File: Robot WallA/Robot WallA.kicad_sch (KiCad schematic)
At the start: 4 parts

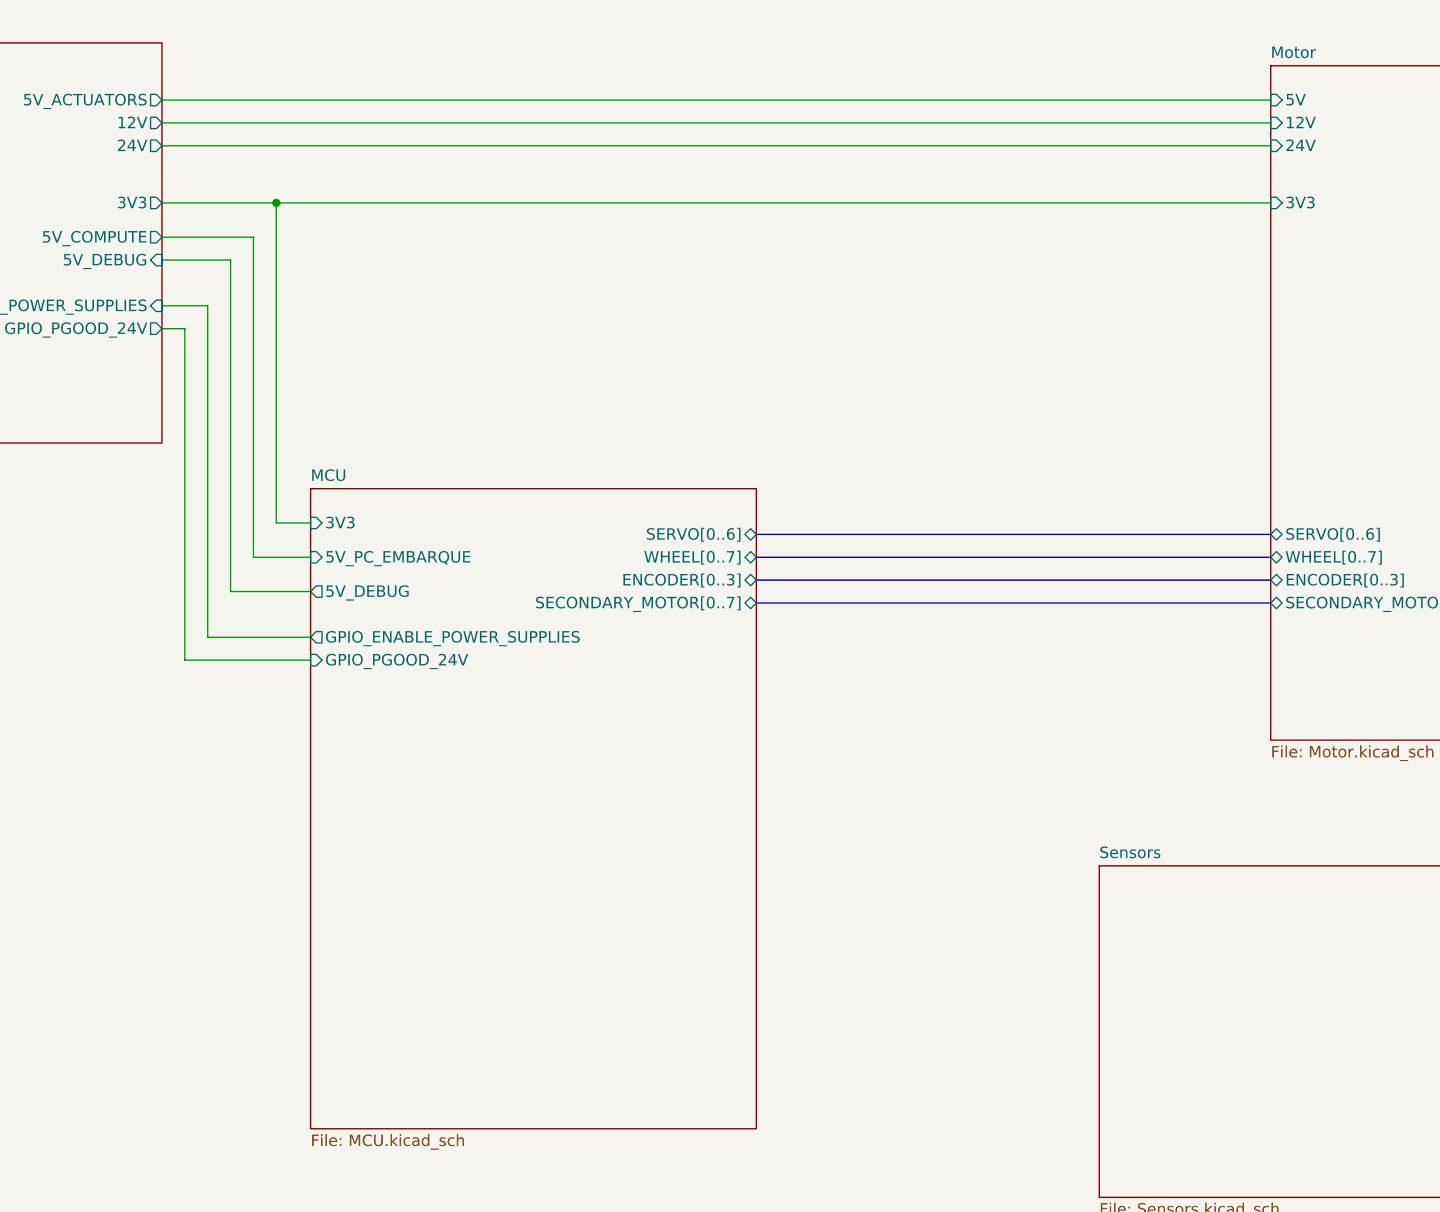
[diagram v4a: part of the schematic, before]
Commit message: Updated USB UART converter, Linked telemeter sensors.
Updated components indicators
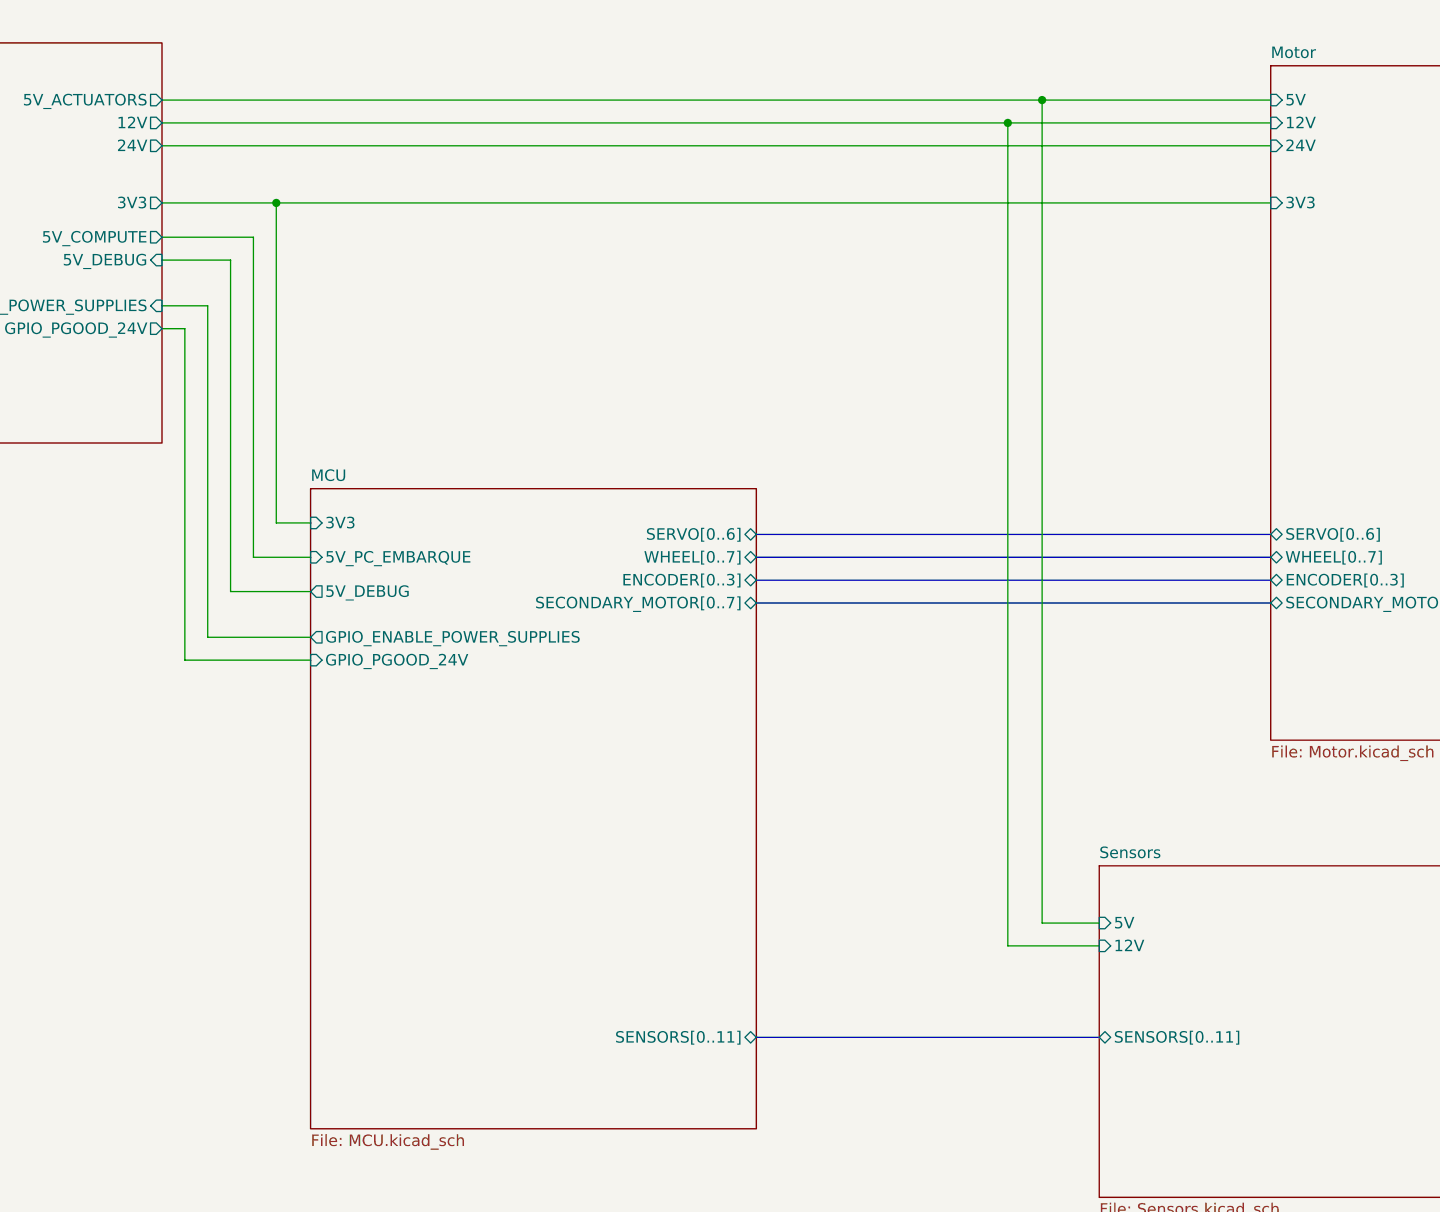
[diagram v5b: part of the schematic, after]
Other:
- sheet MCU ports: added SENSORS[0..11]; removed none
- sheet Sensors ports: added 12V, 5V, SENSORS[0..11]; removed none
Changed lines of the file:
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@@
+	)
+	(junction
+		(at 203.2 25.4)
+		(diameter 0)
+		(color 0 0 0 0)
 	)
 	(junction
@@
 		(color 0 0 0 0)
 	)
-	(wire
-		(pts
-			(xy 109.22 25.4) (xy 232.41 25.4)
+	(junction
+		(at 207.01 22.86)
+		(diameter 0)
+		(color 0 0 0 0)
+	)
+	(wire
+		(pts
+			(xy 109.22 25.4) (xy 203.2 25.4)
 		)
 		(stroke
@@
 	(wire
 		(pts
+			(xy 203.2 25.4) (xy 232.41 25.4)
+		)
+		(stroke
+			(width 0)
+			(type default)
+		)
+	)
+	(wire
+		(pts
 			(xy 109.22 34.29) (xy 121.92 34.29)
 		)
@@
 	(wire
 		(pts
+			(xy 213.36 116.84) (xy 203.2 116.84)
+		)
+		(stroke
+			(width 0)
+			(type default)
+		)
+	)
+	(wire
+		(pts
+			(xy 213.36 114.3) (xy 207.01 114.3)
+		)
+		(stroke
+			(width 0)
+			(type default)
+		)
+	)
+	(wire
+		(pts
 			(xy 125.73 82.55) (xy 114.3 82.55)
 		)
@@
 	(wire
 		(pts
+			(xy 203.2 116.84) (xy 203.2 25.4)
+		)
+		(stroke
+			(width 0)
+			(type default)
+		)
+	)
+	(bus
+		(pts
+			(xy 175.26 127) (xy 213.36 127)
+		)
+		(stroke
+			(width 0)
+			(type default)
+		)
+	)
+	(wire
+		(pts
 			(xy 232.41 34.29) (xy 121.92 34.29)
 		)
@@
 	(wire
 		(pts
+			(xy 207.01 114.3) (xy 207.01 22.86)
+		)
+		(stroke
+			(width 0)
+			(type default)
+		)
+	)
+	(wire
+		(pts
 			(xy 119.38 73.66) (xy 125.73 73.66)
 		)
@@
 	(wire
 		(pts
-			(xy 109.22 22.86) (xy 232.41 22.86)
+			(xy 207.01 22.86) (xy 232.41 22.86)
+		)
+		(stroke
+			(width 0)
+			(type default)
+		)
+	)
+	(wire
+		(pts
+			(xy 109.22 22.86) (xy 207.01 22.86)
 		)
 		(stroke
@@
 			)
 		)
+		(pin "SENSORS[0..11]" bidirectional
+			(at 213.36 127 180)
+			(effects
+				(font
+					(size 1.27 1.27)
+				)
+				(justify left)
+			)
+		)
+		(pin "5V" input
+			(at 213.36 114.3 180)
+			(effects
+				(font
+					(size 1.27 1.27)
+				)
+				(justify left)
+			)
+		)
+		(pin "12V" input
+			(at 213.36 116.84 180)
+			(effects
+				(font
+					(size 1.27 1.27)
+				)
+				(justify left)
+			)
+		)
 		(instances
 			(project "Robot WallA"
@@
 			(effects
 				(font
+					(size 1.27 1.27)
+				)
+				(justify right)
+			)
+		)
+		(pin "SENSORS[0..11]" bidirectional
+			(at 175.26 127 0)
+			(effects
+				(font

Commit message: Added standard switchs, debug leds and 12V and 5V connectors
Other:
- sheet MCU ports: added SENSORS[0..15]; removed SENSORS[0..11]
- sheet Sensors ports: added SENSORS[0..15]; removed SENSORS[0..11]
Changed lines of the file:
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@@
 	(wire
 		(pts
-			(xy 232.41 34.29) (xy 121.92 34.29)
+			(xy 121.92 34.29) (xy 232.41 34.29)
 		)
 		(stroke
@@
 			)
 		)
-		(pin "SENSORS[0..11]" bidirectional
+		(pin "SENSORS[0..15]" bidirectional
 			(at 213.36 127 180)
 			(effects
@@
 			)
 		)
-		(pin "SENSORS[0..11]" bidirectional
+		(pin "SENSORS[0..15]" bidirectional
 			(at 175.26 127 0)
 			(effects

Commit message: Begin to route ethenet, usb, 24V power supply.
Reworked Ethernet sheet because it was too hard to read
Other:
- note added: "Manufacturer: JLCPCB 4 layers 1.6mm 2oz outer layer 0.5oz inner layer https://jlcpcb.com/impedance https://jlcpcb.com/capabilities/pcb-capabilities"
- note added: "PCB Recommendations: FR-4 Glass Epoxy material with 2 oz. (70 μm) copper on both top and bottom layer is recommended for improved thermal performance and better EMI margin (due to lower PCB trace inductance). (From Motor Driver DRV8262 datasheet page 46)"
- note removed: "PCB Recommendations: FR-4 Glass Epoxy material with 2 oz. (70 μm) copper on both top and bottom layer is recommended for improved thermal performance and better EMI margin (due to lower PCB trace inductance). (From Motor Driver DRV8262 datasheet page 47)"
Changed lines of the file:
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@@
 		)
 	)
-	(text "PCB Recommendations:\nFR-4 Glass Epoxy material with 2 oz. (70 μm) copper on both top and bottom layer is recommended for\nimproved thermal performance and better EMI margin (due to lower PCB trace inductance).\n	(From Motor Driver DRV8262 datasheet page 47)"
+	(text "PCB Recommendations:\nFR-4 Glass Epoxy material with 2 oz. (70 μm) copper on both top and bottom layer is recommended for\nimproved thermal performance and better EMI margin (due to lower PCB trace inductance).\n	(From Motor Driver DRV8262 datasheet page 46)"
 		(exclude_from_sim no)
 		(at 226.06 158.242 0)
@@
 				(thickness 0.254)
 				(bold yes)
+			)
+		)
+	)
+	(text "Manufacturer:\nJLCPCB\n4 layers\n1.6mm\n2oz outer layer\n0.5oz inner layer\nhttps://jlcpcb.com/impedance\nhttps://jlcpcb.com/capabilities/pcb-capabilities"
+		(exclude_from_sim no)
+		(at 116.84 177.292 0)
+		(effects
+			(font
+				(size 2 2)
+				(thickness 0.254)
+				(bold yes)

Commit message: Reworked 12V and 5V power supplies, continue routing
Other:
- note added: "Boost 24V 130W --> Pour les moteurs principaux Buck 12V 72W --> Pour les actionneurs Buck 5V Compute 17,5W --> Pour le PC embarqué et le UC Buck 5V Actuators 17,5W --> Pour les actionneurs LDO 3,3V --> Pour le UC"
- note removed: "Boost 24V 130W --> Pour les moteurs principaux Buck 12V 69,6W --> Pour les actionneurs Buck 5V Compute 17,5W --> Pour le PC embarqué et le UC Buck 5V Actuators 17,5W --> Pour les actionneurs LDO 3,3V --> Pour le UC"
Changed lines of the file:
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@@
 		)
 	)
-	(text "Boost 24V 130W --> Pour les moteurs principaux\nBuck 12V 69,6W --> Pour les actionneurs\nBuck 5V Compute   17,5W --> Pour le PC embarqué et le UC\nBuck 5V Actuators 17,5W --> Pour les actionneurs\nLDO 3,3V --> Pour le UC"
+	(text "Boost 24V 130W --> Pour les moteurs principaux\nBuck 12V 72W --> Pour les actionneurs\nBuck 5V Compute   17,5W --> Pour le PC embarqué et le UC\nBuck 5V Actuators 17,5W --> Pour les actionneurs\nLDO 3,3V --> Pour le UC"
 		(exclude_from_sim no)
 		(at 61.468 73.406 0)
